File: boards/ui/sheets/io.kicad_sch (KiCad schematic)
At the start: 16 parts

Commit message: Added schematics docs
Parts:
- renumbered J_VCO2_PITCH1 to J_MIDI_IN2, J_EXT_CUTOFF1 to J_MIDI_IN2
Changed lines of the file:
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@@
 		(on_board yes)
 		(dnp no)
-		(property "Reference" "J_VCO2_PITCH1"
+		(property "Reference" "J_MIDI_IN2"
 			(at 120.65 116.84 0)
 			(effects
@@
 		(on_board yes)
 		(dnp no)
-		(property "Reference" "J_EXT_CUTOFF1"
+		(property "Reference" "J_MIDI_IN2"
 			(at 120.65 140.97 0)
 			(effects

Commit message: Updated MIDI IO
https://github.com/shmoergh/hog/issues/24

UI: Set default pin of PITCH and GATE inputs to MIDI converter's respective outputs
UI: Add 12V power for MIDI2CV converter connector
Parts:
- removed J_MIDI_GNDS1: Conn_01x02, Connector_PinSocket_2.54mm:PinSocket_1x02_P2.54mm_Vertical, symbol Connector_Generic:Conn_01x02
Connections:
- net +5V: no longer J_MIDI_PWR1.2 (Pin_2)
- net GND: now also J_MIDI_PWR1.2 (Pin_2)
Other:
- moved on the sheet: J_MIDI_PWR1

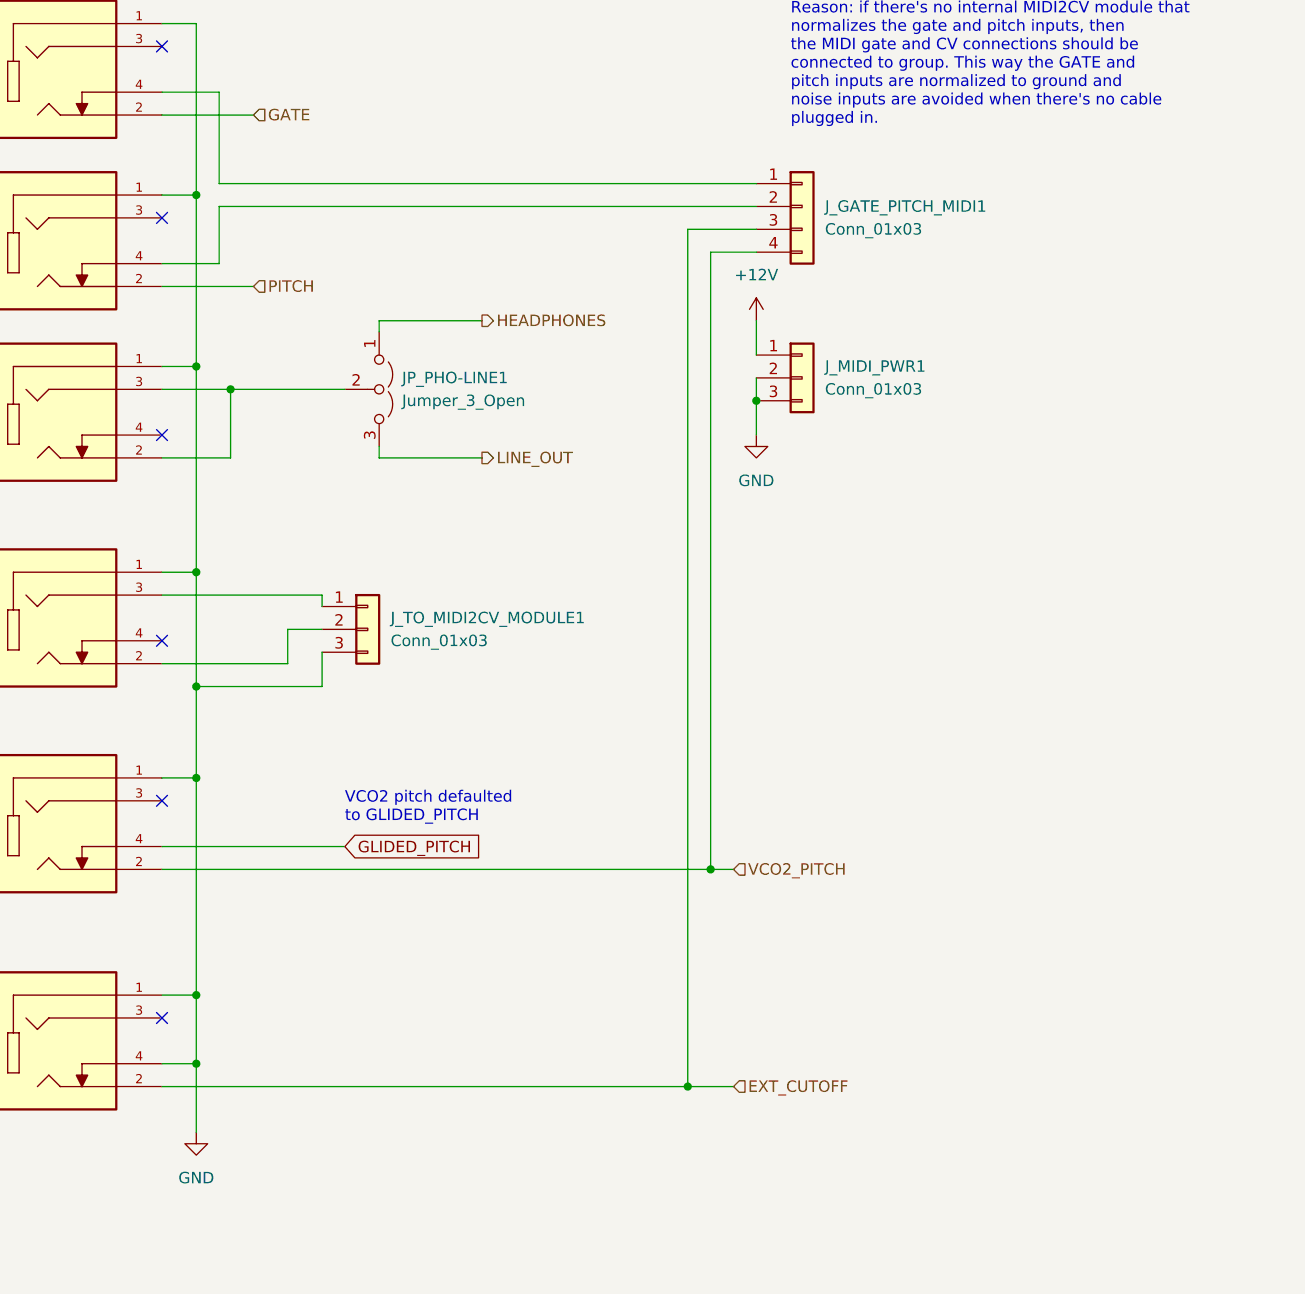
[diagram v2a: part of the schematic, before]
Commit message: Replaced wired MIDI connection to pins
https://github.com/shmoergh/hog/issues/32

MIDI connection was done with manual wired NTS connectors. Now they are replaced with pins and pinheaders just like the other boards.
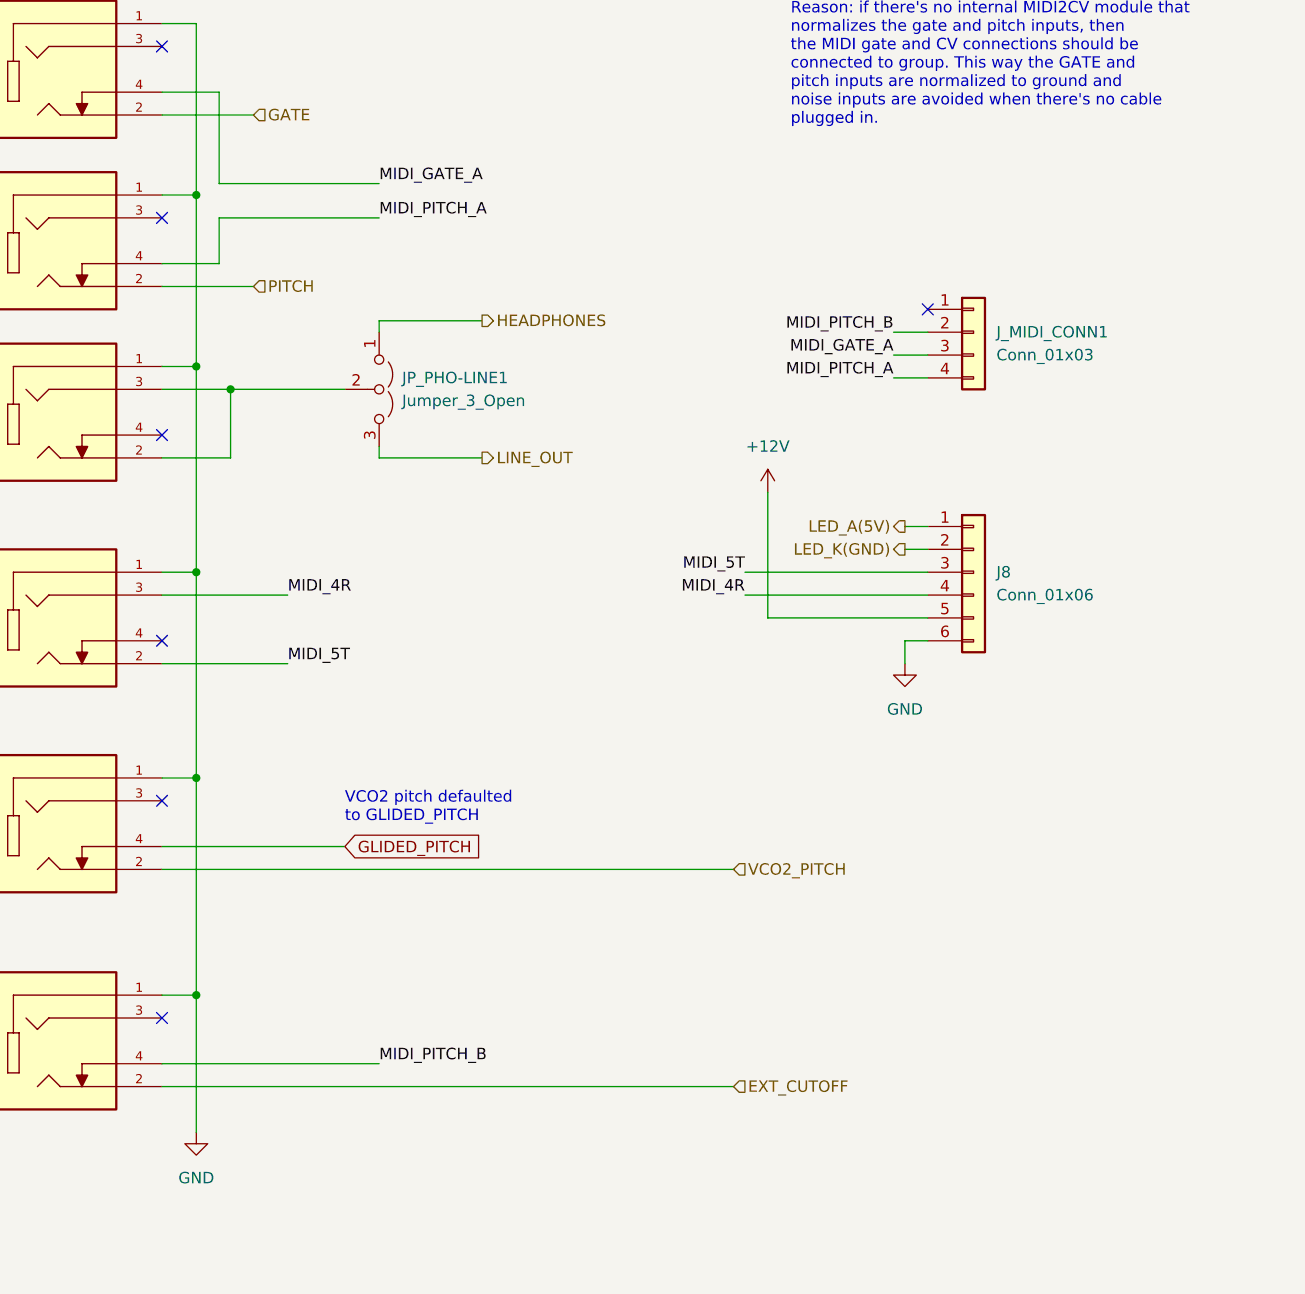
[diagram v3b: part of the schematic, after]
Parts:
- removed J_MIDI_PWR1, J_TO_MIDI2CV_MODULE1: Conn_01x03, Shmoergh_Custom_Footprints:NSL25_01x03_Vertical, symbol Connector_Generic:Conn_01x03
- added J8: Conn_01x06, Connector_PinHeader_2.54mm:PinHeader_1x06_P2.54mm_Vertical, symbol Connector_Generic:Conn_01x06
- J_MIDI_CONN1: renamed from J_GATE_PITCH_MIDI1; footprint Shmoergh_Custom_Footprints:NSL25_01x04_Vertical -> Connector_PinHeader_2.54mm:PinHeader_1x04_P2.54mm_Vertical
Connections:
- net +12V: now also J8.5 (Pin_5)
- net EXT_CUTOFF: no longer J_MIDI_CONN1.3 (Pin_3)
- net GND: now also J8.6 (Pin_6); no longer J_MIDI_IN2.4
- net VCO2_PITCH: no longer J_MIDI_CONN1.4 (Pin_4)
- net MIDI_4R: now reaches J_MIDI_IN1.3
- net MIDI_4R: now also J8.4 (Pin_4)
- net MIDI_5T: now reaches J_MIDI_IN1.2
- net MIDI_5T: now also J8.3 (Pin_3)
- net MIDI_PITCH_A: now reaches J_PITCH1.4
- net MIDI_PITCH_A: now also J_MIDI_CONN1.4 (Pin_4); no longer J_MIDI_CONN1.2 (Pin_2)
- net at J_MIDI_CONN1.1 (Pin_1): no longer J_GATE1.4
- new net LED_A(5V): J8.1 (Pin_1)
- new net LED_K(GND): J8.2 (Pin_2)
- new net MIDI_GATE_A: J_GATE1.4, J_MIDI_CONN1.3 (Pin_3)
- new net MIDI_PITCH_B: J_MIDI_CONN1.2 (Pin_2), J_MIDI_IN2.4
- no-connect marks 6 -> 7
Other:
- moved on the sheet: J_MIDI_CONN1

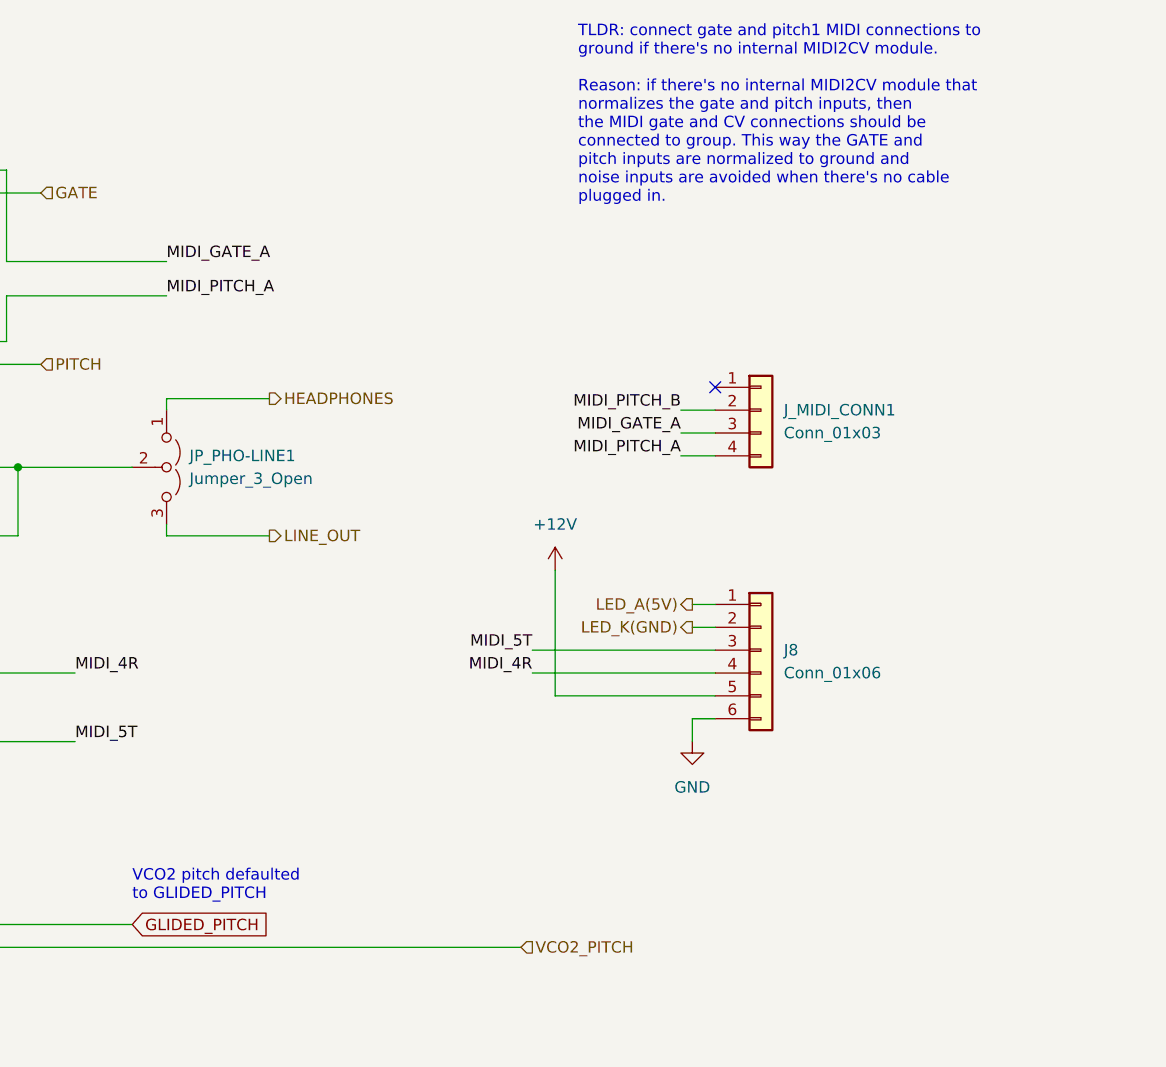
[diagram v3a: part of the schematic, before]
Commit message: Added production files for the UI board
ref https://github.com/shmoergh/hog/issues/19
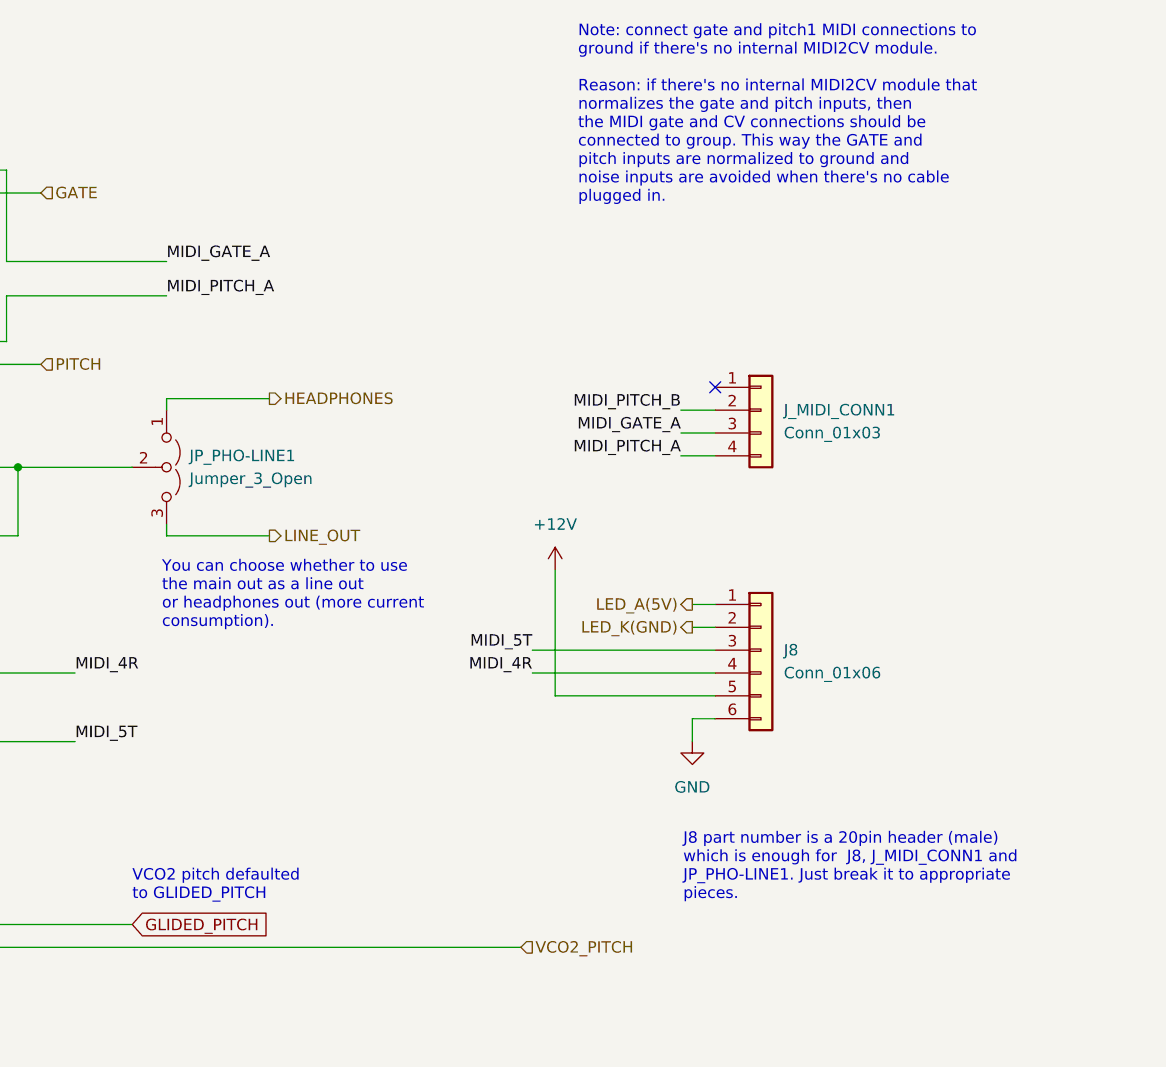
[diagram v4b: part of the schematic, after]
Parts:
- J8: Part No. (none) -> 737-PH1-20-UA; Part URL (none) -> https://mou.sr/4gqTRHQ; Vendor (none) -> Mouser
- JP_PHO-LINE1, J_MIDI_CONN1: now left out of the parts list
- J_GATE1, J_HEADPHONES1, J_MIDI_IN1, J_MIDI_IN2, J_PITCH1: Part No. (none) -> 490-SJ1-3554NG; Part URL (none) -> https://mou.sr/3Qs21VB; Vendor (none) -> Mouser
- R17: Part No. (none) -> 303-MF0W4FF8202B00; Part URL (none) -> https://mou.sr/3Djf3kL; Vendor (none) -> Mouser
- RV_FINE_TUNE1: Component PTD901-1015K-B103 -> (none); Mouser https://mou.sr/4aB7CRn -> (none); Part No. (none) -> PTD901-1015K-B103; Part URL (none) -> https://mou.sr/4aB7CRn; Vendor (none) -> Mouser
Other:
- note added: "J8 part number is a 20pin header (male) which is enough for J8, J_MIDI_CONN1 and JP_PHO-LINE1. Just break it to appropriate pieces."
- note added: "Note: connect gate and pitch1 MIDI connections to ground if there's no internal MIDI2CV module. Reason: if there's no internal MIDI2CV module that normalizes the gate and pitch inputs, then the MIDI gate and CV connections should be connected to group. This way the GATE and pitch inputs are normalized to ground and noise inputs are avoided when there's no cable plugged in."
- note added: "You can choose whether to use the main out as a line out or headphones out (more current consumption)."
- note removed: "TLDR: connect gate and pitch1 MIDI connections to ground if there's no internal MIDI2CV module. Reason: if there's no internal MIDI2CV module that normalizes the gate and pitch inputs, then the MIDI gate and CV connections should be connected to group. This way the GATE and pitch inputs are normalized to ground and noise inputs are avoided when there's no cable plugged in."

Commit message: Updated resistor Mouser no's and added full bom
- Some of the THT resistors in the BOM were referencing to products with min. 1000 pcs order quantity
- Added a full Mouser BOM which can be used to order all Mouser components by uploading to their BOM tool: https://hu.mouser.com/bom/
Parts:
- R17: Part No. 303-MF0W4FF8202B00 -> 603-MFR-25FBF52-82K; Part URL https://mou.sr/3Djf3kL -> https://mou.sr/4bFupx1
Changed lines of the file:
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@@
 	(label "MIDI_GATE_A"
 		(at 231.14 66.04 180)
-		(fields_autoplaced yes)
 		(effects
 			(font
@@
 	(label "MIDI_5T"
 		(at 163.83 100.33 0)
-		(fields_autoplaced yes)
 		(effects
 			(font
@@
 	(label "MIDI_PITCH_B"
 		(at 231.14 63.5 180)
-		(fields_autoplaced yes)
 		(effects
 			(font
@@
 	(label "MIDI_4R"
 		(at 214.63 92.71 180)
-		(fields_autoplaced yes)
 		(effects
 			(font
@@
 	(label "MIDI_PITCH_A"
 		(at 173.99 50.8 0)
-		(fields_autoplaced yes)
 		(effects
 			(font
@@
 	(label "MIDI_4R"
 		(at 163.83 92.71 0)
-		(fields_autoplaced yes)
 		(effects
 			(font
@@
 	(label "MIDI_PITCH_A"
 		(at 231.14 68.58 180)
-		(fields_autoplaced yes)
 		(effects
 			(font
@@
 	(label "MIDI_GATE_A"
 		(at 173.99 46.99 0)
-		(fields_autoplaced yes)
 		(effects
 			(font
@@
 	(label "MIDI_5T"
 		(at 214.63 90.17 180)
-		(fields_autoplaced yes)
 		(effects
 			(font
@@
 	(label "MIDI_PITCH_B"
 		(at 173.99 144.78 0)
-		(fields_autoplaced yes)
 		(effects
 			(font
@@
 		(shape input)
 		(at 59.69 88.9 180)
-		(fields_autoplaced yes)
 		(effects
 			(font
@@
 		(shape output)
 		(at 185.42 77.47 0)
-		(fields_autoplaced yes)
 		(effects
 			(font
@@
 		(shape input)
 		(at 160.02 58.42 0)
-		(fields_autoplaced yes)
 		(effects
 			(font
@@
 		(shape output)
 		(at 232.41 87.63 180)
-		(fields_autoplaced yes)
 		(effects
 			(font
@@
 		(shape input)
 		(at 160.02 39.37 0)
-		(fields_autoplaced yes)
 		(effects
 			(font
@@
 		(shape output)
 		(at 232.41 85.09 180)
-		(fields_autoplaced yes)
 		(effects
 			(font
@@
 		(shape input)
 		(at 213.36 123.19 0)
-		(fields_autoplaced yes)
 		(effects
 			(font
@@
 		(shape input)
 		(at 213.36 147.32 0)
-		(fields_autoplaced yes)
 		(effects
 			(font
@@
 		(shape output)
 		(at 185.42 62.23 0)
-		(fields_autoplaced yes)
 		(effects
 			(font
@@
 			)
 		)
-		(property "Part No." "303-MF0W4FF8202B00 "
+		(property "Part No." "603-MFR-25FBF52-82K "
 			(at 67.31 78.74 0)
 			(effects
@@
 			)
 		)
-		(property "Part URL" "https://mou.sr/3Djf3kL"
+		(property "Part URL" "https://mou.sr/4bFupx1"
 			(at 67.31 78.74 0)
 			(effects
@@
 			)
 		)
-		(property "Part No." "303-MF0W4FF8202B00 "
+		(property "Part No." "603-MFR-25FBF52-82K "
 			(at 67.31 99.06 0)
 			(effects
@@
 			)
 		)
-		(property "Part URL" "https://mou.sr/3Djf3kL"
+		(property "Part URL" "https://mou.sr/4bFupx1"
 			(at 67.31 99.06 0)
 			(effects
